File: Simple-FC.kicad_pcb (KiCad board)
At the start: 2 copper layers, 40 x 40 mm, 76 parts, among them J1 USB_C_Receptacle_USB2.0_14P, J10 Conn_01x01, J2 Micro_SD_Card, J3 Conn_01x04, J4 Conn_01x04, J5 Conn_01x04, J6 Conn_01x05, J7 Conn_01x04, J8 Conn_01x03, J9 Conn_01x01, SW1 SW_Push, U1 RP2350A, U2 MMC5983MA, U3 LSM6DSM, U4 BMP384, U5 TPS631000, U6 W25Q128JVS, Y1 ABM8-272-T3

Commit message: routed up ICs
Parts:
- moved R6 95.2 mm to (158.8, 116.8), turned to 180 degrees
- moved R7 95.0 mm to (158.8, 117.9), turned to 180 degrees
- moved C17 91.4 mm to (154.9, 110.3), turned to 180 degrees
- moved C22 90.9 mm to (159.4, 105.1), turned to 90 degrees
- moved R19 90.9 mm to (160.2, 114.6)
- moved R18 90.7 mm to (160.2, 112.0)
- moved C23 89.3 mm to (157.9, 106.5), turned to 180 degrees
- moved C18 88.8 mm to (153.0, 110.3)
- moved R1 87.0 mm to (152.9, 94.0), turned to -90 degrees
- moved R8 86.0 mm to (150.9, 110.9), turned to -90 degrees
- moved C25 85.0 mm to (156.2, 97.1), turned to 180 degrees
- moved R2 83.7 mm to (149.9, 93.3), turned to 180 degrees
- moved R9 83.4 mm to (148.8, 110.9), turned to -90 degrees
- moved R10 81.7 mm to (147.7, 110.9), turned to -90 degrees
- moved C26 80.5 mm to (151.3, 99.5)
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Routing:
- net +3V3: track 23.3 -> 47.0 mm, vias 3 -> 21
- net GND: track 3.50 -> 11.9 mm, vias 3 -> 7
- net /SD_MISO: track 0.00 -> 6.32 mm
- net /SD_SCLK: track 0.00 -> 5.98 mm
- net Net-(J2-DAT2): track 0.00 -> 5.95 mm
- net /SD_MOSI: track 0.00 -> 5.94 mm
- net /SD_CS: track 0.00 -> 5.93 mm
- net Net-(J2-DAT1): track 0.00 -> 4.22 mm
- net /QSPI_SS: track 7.70 -> 11.1 mm
- net Net-(U1-VREG_AVDD): track 0.00 -> 3.03 mm
- net VBUS: track 7.80 -> 10.8 mm
- net Net-(R3-Pad1): track 0.00 -> 2.50 mm
- net /SDA: track 0.00 -> 2.31 mm
- net /SCL: track 0.00 -> 2.29 mm
- net Net-(J1-CC1): track 0.00 -> 2.23 mm
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- added copper zone on F.Cu, net +3V3

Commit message: added power trace
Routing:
- net Net-(D2-A): track 0.00 -> 3.50 mm
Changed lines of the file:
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@@
+	)
+	(segment
+		(start 135.75 123.45)
+		(end 135.75 121.15)
+		(width 0.6)
+		(layer "F.Cu")
+		(net "Net-(D2-A)")
+	)
+	(segment
+		(start 135.75 121.15)
+		(end 134.9 120.3)
+		(width 0.6)
+		(layer "F.Cu")
+		(net "Net-(D2-A)")
 	)
 	(segment

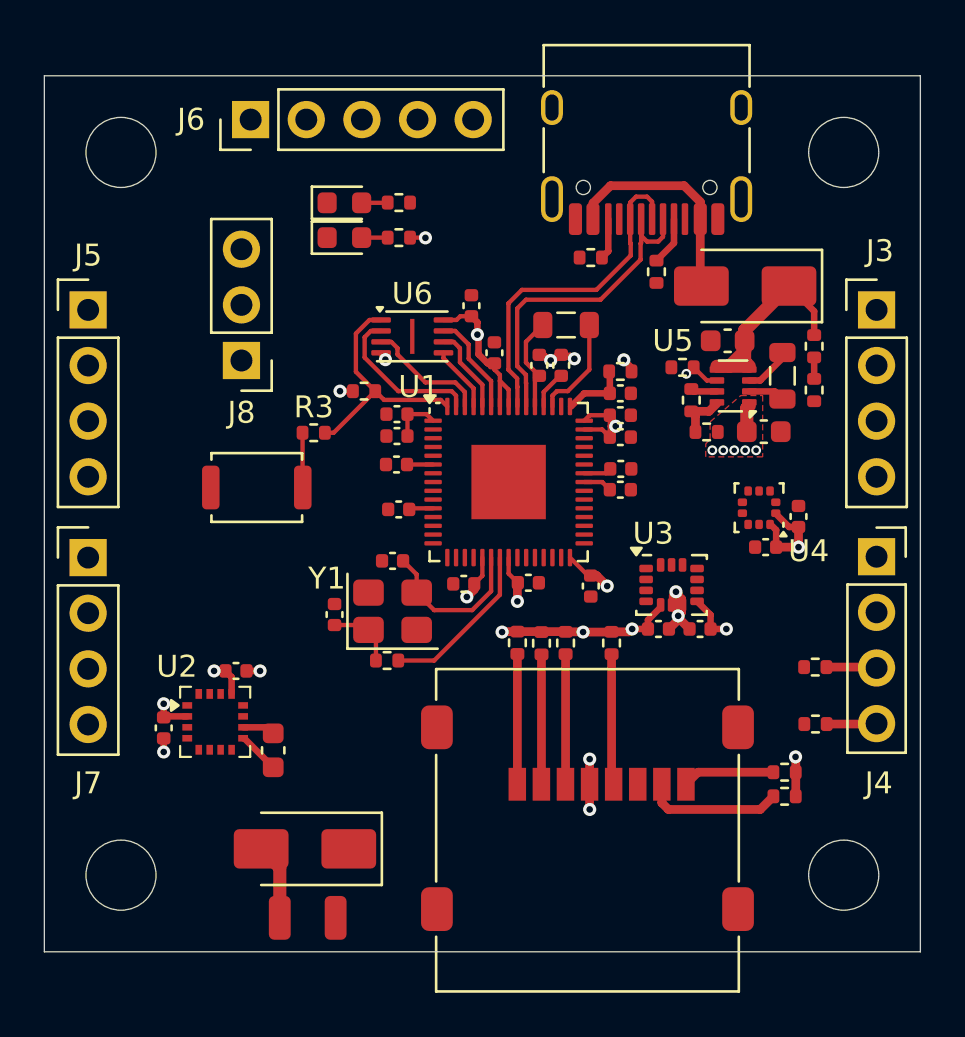
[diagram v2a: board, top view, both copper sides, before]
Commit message: finished routing pcb
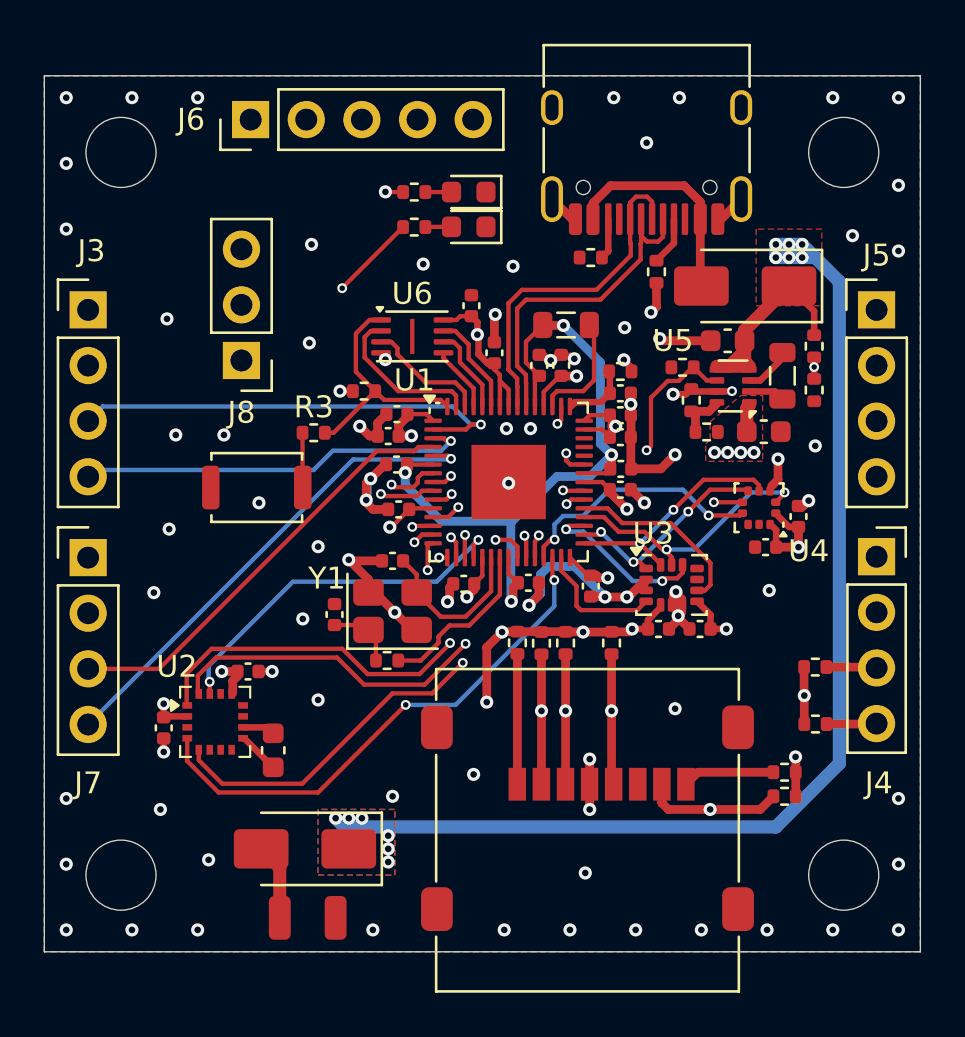
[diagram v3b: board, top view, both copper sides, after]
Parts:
- moved J3 36.0 mm to (127.0, 95.7)
- moved J5 36.0 mm to (163.0, 95.7)
- moved D4 6.05 mm to (144.4, 90.3), turned to 180 degrees
- moved D3 5.78 mm to (144.4, 91.9), turned to 180 degrees
- moved R21 2.20 mm to (141.9, 90.3), turned to 0 degrees
- moved R20 1.32 mm to (141.9, 91.9), turned to 0 degrees
- moved C21 0.55 mm to (134.3, 112.2)
- moved C4 0.40 mm to (140.7, 101.5)
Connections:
- J1 pad SH: (no net) -> GND
- J3 pad 1: +3.3V -> +3V3
- J4 pad 1: +3.3V -> +3V3
- J5 pad 1: +3.3V -> +3V3
- J7 pad 1: +3.3V -> +3V3
- R21 pad 1: +3.3V -> +3V3
- U1 pad 19: unconnected-(U1-GPIO15-Pad19) -> /MMC_INT
- U1 pad 27: unconnected-(U1-GPIO16-Pad27) -> /BMP_INT
- U1 pad 29: unconnected-(U1-GPIO18-Pad29) -> /LSM_INT1
- U1 pad 33: /LMS_CS -> /LSM_CS
- U1 pad 35: unconnected-(U1-GPIO23-Pad35) -> /LSM_INT2
- U3 pad 14: /MISO -> /MOSI
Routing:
- net /SDA: track 2.31 -> 65.8 mm
- net /SCL: track 2.29 -> 65.1 mm, vias 0 -> 1
- net VBUS: track 10.8 -> 63.2 mm, vias 0 -> 12
- net GND: track 11.9 -> 56.6 mm, vias 7 -> 80
- net +3V3: track 47.0 -> 91.2 mm, vias 21 -> 28
- net /SCLK: track 0.00 -> 40.1 mm, vias 0 -> 3
- net /MOSI: track 0.00 -> 35.8 mm, vias 0 -> 3
- net /MISO: track 0.00 -> 35.4 mm, vias 0 -> 4
- net /SWDIO: track 0.00 -> 24.7 mm, vias 0 -> 1
- net +1V1: track 9.05 -> 33.6 mm, vias 1 -> 4
- net /PWM0: track 0.00 -> 24.4 mm, vias 0 -> 1
- net /MMC_CS: track 0.00 -> 24.2 mm, vias 0 -> 2
- net /PWM3: track 0.00 -> 22.9 mm, vias 0 -> 1
- net /PWM2: track 0.00 -> 21.1 mm, vias 0 -> 1
- net /UART0_TX: track 0.00 -> 20.8 mm, vias 0 -> 1
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- added copper zone on In2.Cu, net +3V3
- added copper zone on B.Cu, net GND
- added copper zone on F.Cu, net GND
- added copper zone on B.Cu, net VBUS
- added copper zone on F.Cu, net VBUS
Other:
- copper layers 2 -> 4

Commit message: fixed pin footprint
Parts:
- J4: footprint Connector_PinSocket_2.54mm:PinSocket_1x04_P2.54mm_Vertical -> Connector_PinHeader_2.54mm:PinHeader_1x04_P2.54mm_Vertical

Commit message: touched up pcb
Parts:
- moved R6 14.5 mm to (145.8, 110.3), turned to -90 degrees
- moved R7 14.2 mm to (146.8, 110.3), turned to -90 degrees
- moved R11 14.0 mm to (158.7, 118.0), turned to 180 degrees
- moved R10 12.5 mm to (158.7, 116.9), turned to 180 degrees
- moved C19 4.17 mm to (134.1, 111.8), turned to 0 degrees
- moved C21 3.88 mm to (130.5, 113.0), turned to 90 degrees
- moved C20 3.35 mm to (133.1, 116.8), turned to 0 degrees
- moved R8 2.38 mm to (148.6, 110.3)
- moved R9 1.51 mm to (150.3, 110.7), turned to 0 degrees
- moved J2 0.65 mm to (149.8, 118.8), turned to 180 degrees
- turned U2 to 90 degrees
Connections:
- U2 pad 11: unconnected-(U2-GND-Pad11) -> GND
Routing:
- net +3V3: track 91.2 -> 101.2 mm, vias 28 -> 29
- net /SD_CS: track 20.0 -> 29.9 mm
- net /SD_MISO: track 25.4 -> 18.1 mm
- net /SD_MOSI: track 17.3 -> 23.6 mm
- net Net-(J2-DAT1): track 4.22 -> 10.3 mm
- net /MMC_INT: track 16.9 -> 21.7 mm
- net /MISO: track 35.4 -> 31.6 mm
- net /SDA: track 65.8 -> 69.5 mm
- net /SCL: track 65.1 -> 68.5 mm
- net /MOSI: track 35.8 -> 39.1 mm
- net /MMC_CS: track 24.2 -> 21.0 mm
- net /SD_SCLK: track 18.8 -> 20.3 mm
- net GND: track 56.6 -> 57.0 mm, vias 80 -> 84
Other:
- board text added: "+"
- board text added: "-"
- board text added: "0"
- board text added: "1"
- board text added: "1.2V-5.3V"
- board text added: "2"
- board text added: "3"
- board text added: "CLK"
- board text added: "ESC"
- board text added: "I2C"
- board text added: "IO"
- board text added: "RX"
- board text added: "SCL"
- board text added: "SDA"
- board text added: "TX"
- board text added: "UART0"
- board text added: "UART1"
- board text added: "X"
- board text added: "Y"
